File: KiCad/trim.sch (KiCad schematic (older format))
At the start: 33 parts

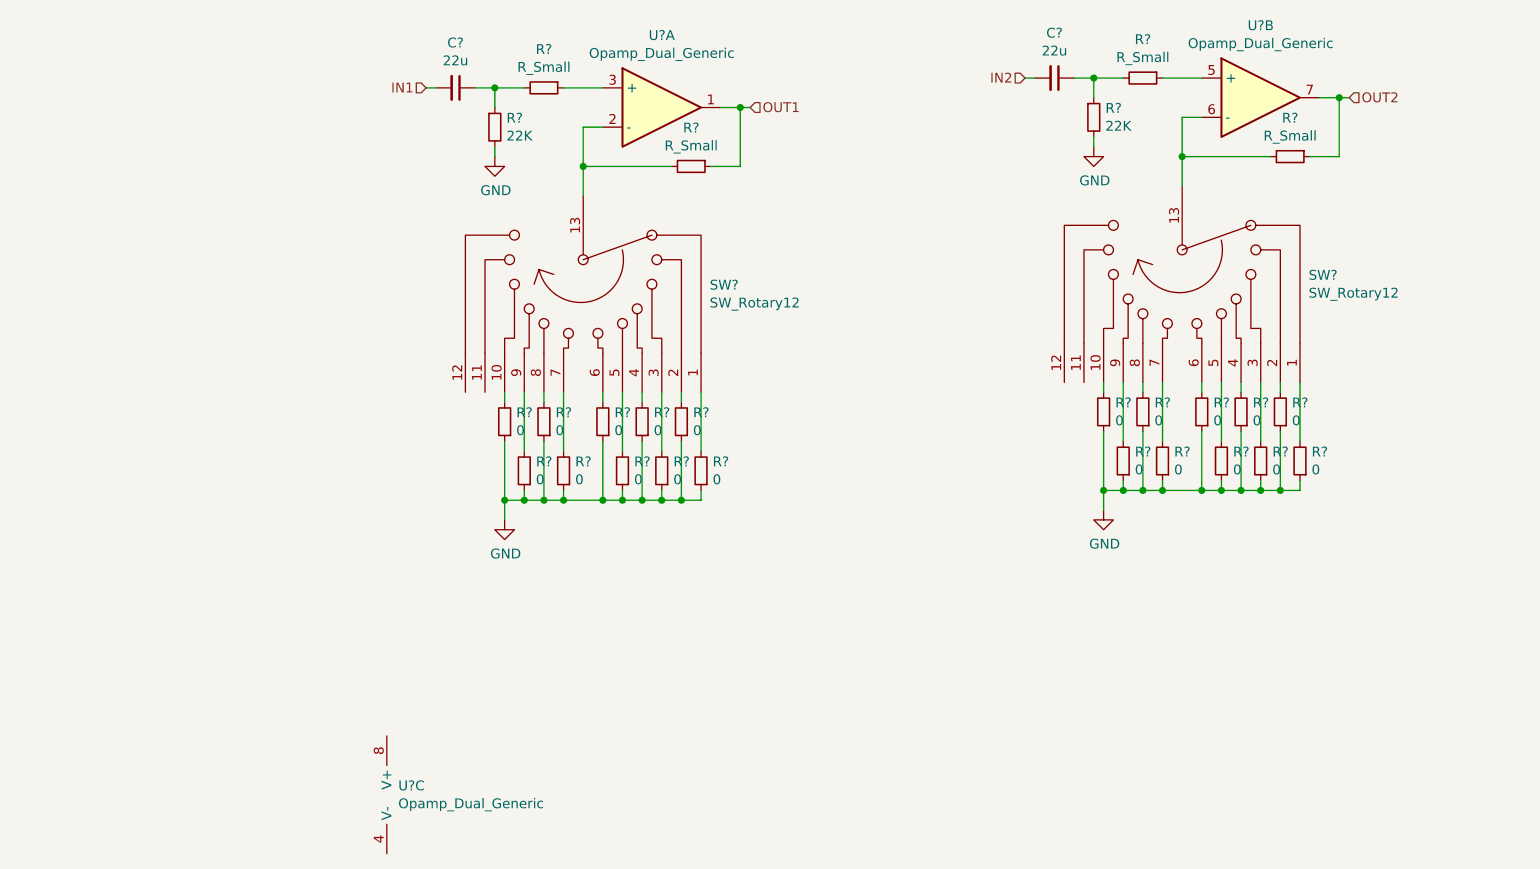
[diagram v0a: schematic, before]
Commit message: restored filter and added initial attenuation in trim
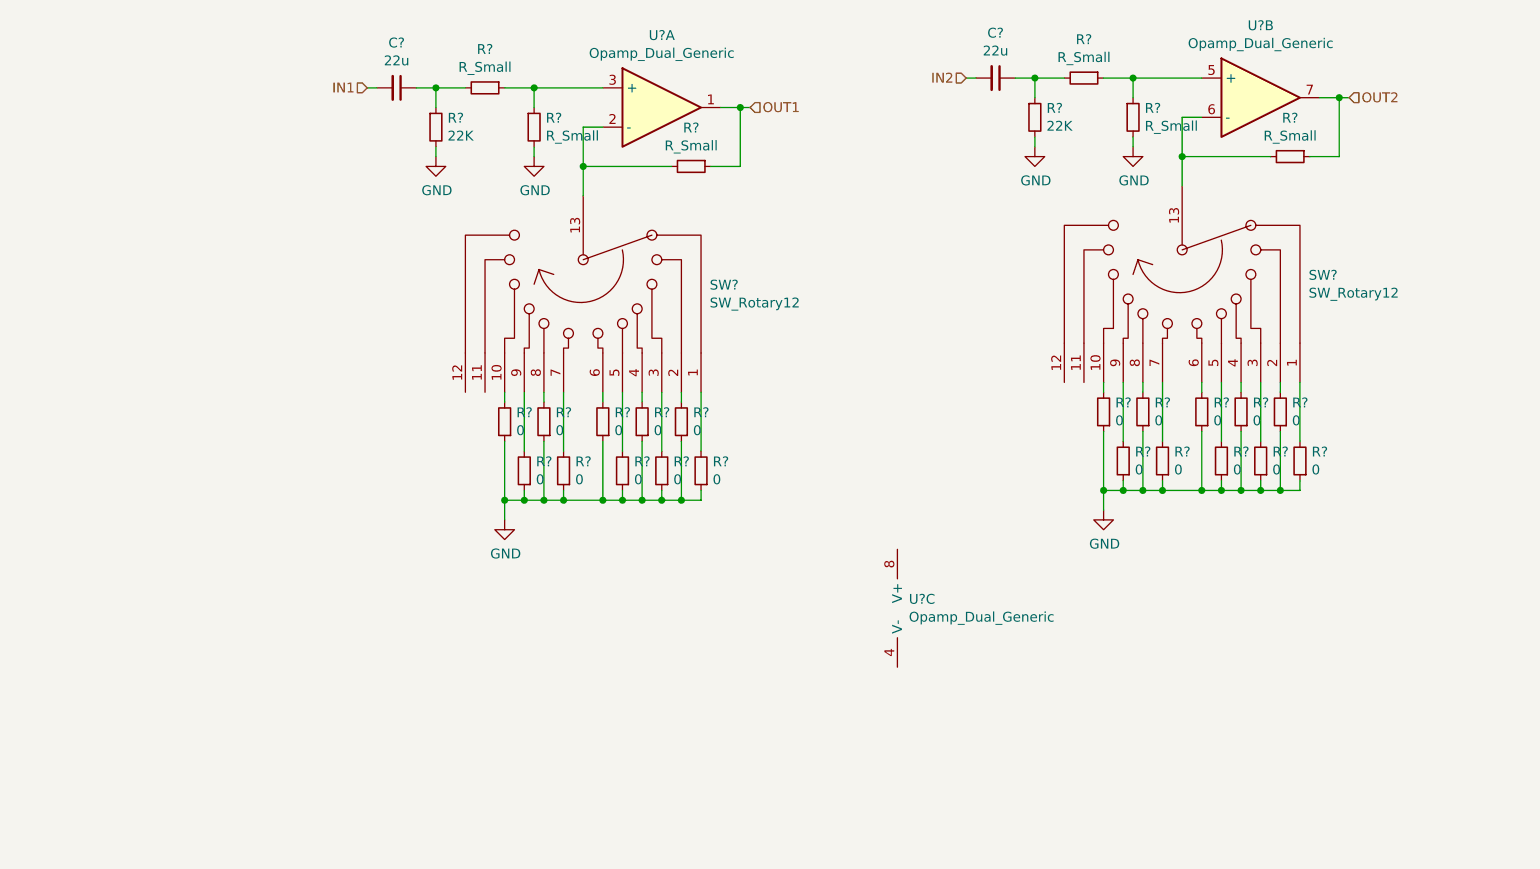
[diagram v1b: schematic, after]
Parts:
- removed R?: 22K, symbol Device:R_Small
- removed R?: R_Small, symbol Device:R_Small
- added R? (x3): R_Small, symbol Device:R_Small
- added R?: 22K, symbol Device:R_Small
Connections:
- net GND: now also R?.2, R?.2, R?.2
- net at R?.1, U?.3 (+): now also R?.1
- net at C?.1: now also R?.1, R?.2
- net at U?.5 (+): now also R?.1, R?.1
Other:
- moved on the sheet: C?, R?, U?C
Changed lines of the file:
@@
 $Descr A4 11693 8268
 encoding utf-8
-Sheet 4 4
+Sheet 4 5
 Title ""
 Date ""
@@
 L Device:C_Small C?
 U 1 1 60412D0A
-P 3650 3000
-F 0 "C?" V 3421 3000 50  0000 C CNN
-F 1 "22u" V 3512 3000 50  0000 C CNN
-F 2 "" H 3650 3000 50  0001 C CNN
-F 3 "~" H 3650 3000 50  0001 C CNN
-	1    3650 3000
+P 3350 3000
+F 0 "C?" V 3121 3000 50  0000 C CNN
+F 1 "22u" V 3212 3000 50  0000 C CNN
+F 2 "" H 3350 3000 50  0001 C CNN
+F 3 "~" H 3350 3000 50  0001 C CNN
+	1    3350 3000
 	0    1    1    0
 $EndComp
@@
 L Device:R_Small R?
 U 1 1 6041330E
-P 3850 3200
-F 0 "R?" H 3909 3246 50  0000 L CNN
-F 1 "22K" H 3909 3155 50  0000 L CNN
-F 2 "" H 3850 3200 50  0001 C CNN
-F 3 "~" H 3850 3200 50  0001 C CNN
-	1    3850 3200
-	1    0    0    -1
-$EndComp
-Wire Wire Line
-	3850 3100 3850 3000
-Wire Wire Line
-	3850 3000 3750 3000
+P 3550 3200
+F 0 "R?" H 3609 3246 50  0000 L CNN
+F 1 "22K" H 3609 3155 50  0000 L CNN
+F 2 "" H 3550 3200 50  0001 C CNN
+F 3 "~" H 3550 3200 50  0001 C CNN
+	1    3550 3200
+	1    0    0    -1
+$EndComp
+Wire Wire Line
+	3550 3100 3550 3000
+Wire Wire Line
+	3550 3000 3450 3000
 $Comp
 L power:GND #PWR?
 U 1 1 6041385B
-P 3850 3350
-F 0 "#PWR?" H 3850 3100 50  0001 C CNN
-F 1 "GND" H 3855 3177 50  0000 C CNN
-F 2 "" H 3850 3350 50  0001 C CNN
-F 3 "" H 3850 3350 50  0001 C CNN
-	1    3850 3350
-	1    0    0    -1
-$EndComp
-Wire Wire Line
-	3850 3350 3850 3300
+P 3550 3350
+F 0 "#PWR?" H 3550 3100 50  0001 C CNN
+F 1 "GND" H 3555 3177 50  0000 C CNN
+F 2 "" H 3550 3350 50  0001 C CNN
+F 3 "" H 3550 3350 50  0001 C CNN
+	1    3550 3350
+	1    0    0    -1
+$EndComp
+Wire Wire Line
+	3550 3350 3550 3300
 $Comp
 L Device:R_Small R?
 U 1 1 60413A53
-P 4100 3000
-F 0 "R?" V 3904 3000 50  0000 C CNN
-F 1 "R_Small" V 3995 3000 50  0000 C CNN
-F 2 "" H 4100 3000 50  0001 C CNN
-F 3 "~" H 4100 3000 50  0001 C CNN
-	1    4100 3000
-	0    1    1    0
-$EndComp
-Wire Wire Line
-	4000 3000 3850 3000
-Connection ~ 3850 3000
+P 3800 3000
+F 0 "R?" V 3604 3000 50  0000 C CNN
+F 1 "R_Small" V 3695 3000 50  0000 C CNN
+F 2 "" H 3800 3000 50  0001 C CNN
+F 3 "~" H 3800 3000 50  0001 C CNN
+	1    3800 3000
+	0    1    1    0
+$EndComp
+Connection ~ 3550 3000
 $Comp
 L Device:Opamp_Dual_Generic U?
@@
 $EndComp
 Wire Wire Line
-	4400 3000 4200 3000
-Wire Wire Line
 	4400 3200 4300 3200
 Wire Wire Line
@@
 L Device:C_Small C?
 U 1 1 604284FE
-P 6700 2950
-F 0 "C?" V 6471 2950 50  0000 C CNN
-F 1 "22u" V 6562 2950 50  0000 C CNN
-F 2 "" H 6700 2950 50  0001 C CNN
-F 3 "~" H 6700 2950 50  0001 C CNN
-	1    6700 2950
-	0    1    1    0
-$EndComp
-$Comp
-L Device:R_Small R?
-U 1 1 60428504
-P 6900 3150
-F 0 "R?" H 6959 3196 50  0000 L CNN
-F 1 "22K" H 6959 3105 50  0000 L CNN
-F 2 "" H 6900 3150 50  0001 C CNN
-F 3 "~" H 6900 3150 50  0001 C CNN
-	1    6900 3150
-	1    0    0    -1
-$EndComp
-Wire Wire Line
-	6900 3050 6900 2950
-Wire Wire Line
-	6900 2950 6800 2950
-$Comp
-L power:GND #PWR?
-U 1 1 6042850C
-P 6900 3300
-F 0 "#PWR?" H 6900 3050 50  0001 C CNN
-F 1 "GND" H 6905 3127 50  0000 C CNN
-F 2 "" H 6900 3300 50  0001 C CNN
-F 3 "" H 6900 3300 50  0001 C CNN
-	1    6900 3300
-	1    0    0    -1
-$EndComp
-Wire Wire Line
-	6900 3300 6900 3250
-$Comp
-L Device:R_Small R?
-U 1 1 60428513
-P 7150 2950
-F 0 "R?" V 6954 2950 50  0000 C CNN
-F 1 "R_Small" V 7045 2950 50  0000 C CNN
-F 2 "" H 7150 2950 50  0001 C CNN
-F 3 "~" H 7150 2950 50  0001 C CNN
-	1    7150 2950
-	0    1    1    0
-$EndComp
-Wire Wire Line
-	7050 2950 6900 2950
-Connection ~ 6900 2950
-Wire Wire Line
-	7450 2950 7250 2950
+P 6400 2950
+F 0 "C?" V 6171 2950 50  0000 C CNN
+F 1 "22u" V 6262 2950 50  0000 C CNN
+F 2 "" H 6400 2950 50  0001 C CNN
+F 3 "~" H 6400 2950 50  0001 C CNN
+	1    6400 2950
+	0    1    1    0
+$EndComp
 Wire Wire Line
 	7450 3150 7350 3150
@@
 Wire Wire Line
 	6950 5050 7050 5050
-Text HLabel 3500 3000 0    50   Input ~ 0
+Text HLabel 3200 3000 0    50   Input ~ 0
 IN1
 Wire Wire Line
-	3500 3000 3550 3000
+	3200 3000 3250 3000
 Text HLabel 5150 3100 2    50   Input ~ 0
 OUT1
@@
 	5150 3100 5100 3100
 Connection ~ 5100 3100
-Text HLabel 6550 2950 0    50   Input ~ 0
+Text HLabel 6250 2950 0    50   Input ~ 0
 IN2
 Wire Wire Line
-	6550 2950 6600 2950
+	6250 2950 6300 2950
 Text HLabel 8200 3050 2    50   Input ~ 0
 OUT2
@@
 L Device:Opamp_Dual_Generic U?
 U 3 1 60459ACB
-P 3400 6600
-F 0 "U?" H 3358 6646 50  0000 L CNN
-F 1 "Opamp_Dual_Generic" H 3358 6555 50  0000 L CNN
-F 2 "" H 3400 6600 50  0001 C CNN
-F 3 "~" H 3400 6600 50  0001 C CNN
-	3    3400 6600
-	1    0    0    -1
-$EndComp
+P 6000 5650
+F 0 "U?" H 5958 5696 50  0000 L CNN
+F 1 "Opamp_Dual_Generic" H 5958 5605 50  0000 L CNN
+F 2 "" H 6000 5650 50  0001 C CNN
+F 3 "~" H 6000 5650 50  0001 C CNN
+	3    6000 5650
+	1    0    0    -1
+$EndComp
+$Comp
+L Device:R_Small R?
+U 1 1 6049EE8B
+P 4050 3200
+F 0 "R?" H 4109 3246 50  0000 L CNN
+F 1 "R_Small" H 4109 3155 50  0000 L CNN
+F 2 "" H 4050 3200 50  0001 C CNN
+F 3 "~" H 4050 3200 50  0001 C CNN
+	1    4050 3200
+	1    0    0    -1
+$EndComp
+Wire Wire Line
+	4050 3100 4050 3000
+$Comp
+L power:GND #PWR?
+U 1 1 6049EE92
+P 4050 3350
+F 0 "#PWR?" H 4050 3100 50  0001 C CNN
+F 1 "GND" H 4055 3177 50  0000 C CNN
+F 2 "" H 4050 3350 50  0001 C CNN
+F 3 "" H 4050 3350 50  0001 C CNN
+	1    4050 3350
+	1    0    0    -1
+$EndComp
+Wire Wire Line
+	4050 3350 4050 3300
+Wire Wire Line
+	3900 3000 4050 3000
+Connection ~ 4050 3000
+Wire Wire Line
+	4050 3000 4400 3000
+Wire Wire Line
+	3550 3000 3700 3000
+$Comp
+L Device:R_Small R?
+U 1 1 604B93C5
+P 6600 3150
+F 0 "R?" H 6659 3196 50  0000 L CNN
+F 1 "22K" H 6659 3105 50  0000 L CNN
+F 2 "" H 6600 3150 50  0001 C CNN
+F 3 "~" H 6600 3150 50  0001 C CNN
+	1    6600 3150
+	1    0    0    -1
+$EndComp
+Wire Wire Line
+	6600 3050 6600 2950
+Wire Wire Line
+	6600 2950 6500 2950
+$Comp
+L power:GND #PWR?
+U 1 1 604B93CD
+P 6600 3300
+F 0 "#PWR?" H 6600 3050 50  0001 C CNN
+F 1 "GND" H 6605 3127 50  0000 C CNN
+F 2 "" H 6600 3300 50  0001 C CNN
+F 3 "" H 6600 3300 50  0001 C CNN
+	1    6600 3300
+	1    0    0    -1
+$EndComp
+Wire Wire Line
+	6600 3300 6600 3250
+$Comp
+L Device:R_Small R?
+U 1 1 604B93D4
+P 6850 2950
+F 0 "R?" V 6654 2950 50  0000 C CNN
+F 1 "R_Small" V 6745 2950 50  0000 C CNN
+F 2 "" H 6850 2950 50  0001 C CNN
+F 3 "~" H 6850 2950 50  0001 C CNN
+	1    6850 2950
+	0    1    1    0
+$EndComp
+Connection ~ 6600 2950
+$Comp
+L Device:R_Small R?
+U 1 1 604B93DB
+P 7100 3150
+F 0 "R?" H 7159 3196 50  0000 L CNN
+F 1 "R_Small" H 7159 3105 50  0000 L CNN
+F 2 "" H 7100 3150 50  0001 C CNN
+F 3 "~" H 7100 3150 50  0001 C CNN
+	1    7100 3150
+	1    0    0    -1
+$EndComp
+Wire Wire Line
+	7100 3050 7100 2950
+$Comp
+L power:GND #PWR?
+U 1 1 604B93E2
+P 7100 3300
+F 0 "#PWR?" H 7100 3050 50  0001 C CNN
+F 1 "GND" H 7105 3127 50  0000 C CNN
+F 2 "" H 7100 3300 50  0001 C CNN
+F 3 "" H 7100 3300 50  0001 C CNN
+	1    7100 3300
+	1    0    0    -1
+$EndComp
+Wire Wire Line
+	7100 3300 7100 3250
+Wire Wire Line
+	6950 2950 7100 2950
+Connection ~ 7100 2950
+Wire Wire Line
+	7100 2950 7450 2950
+Wire Wire Line
+	6600 2950 6750 2950
 $EndSCHEMATC

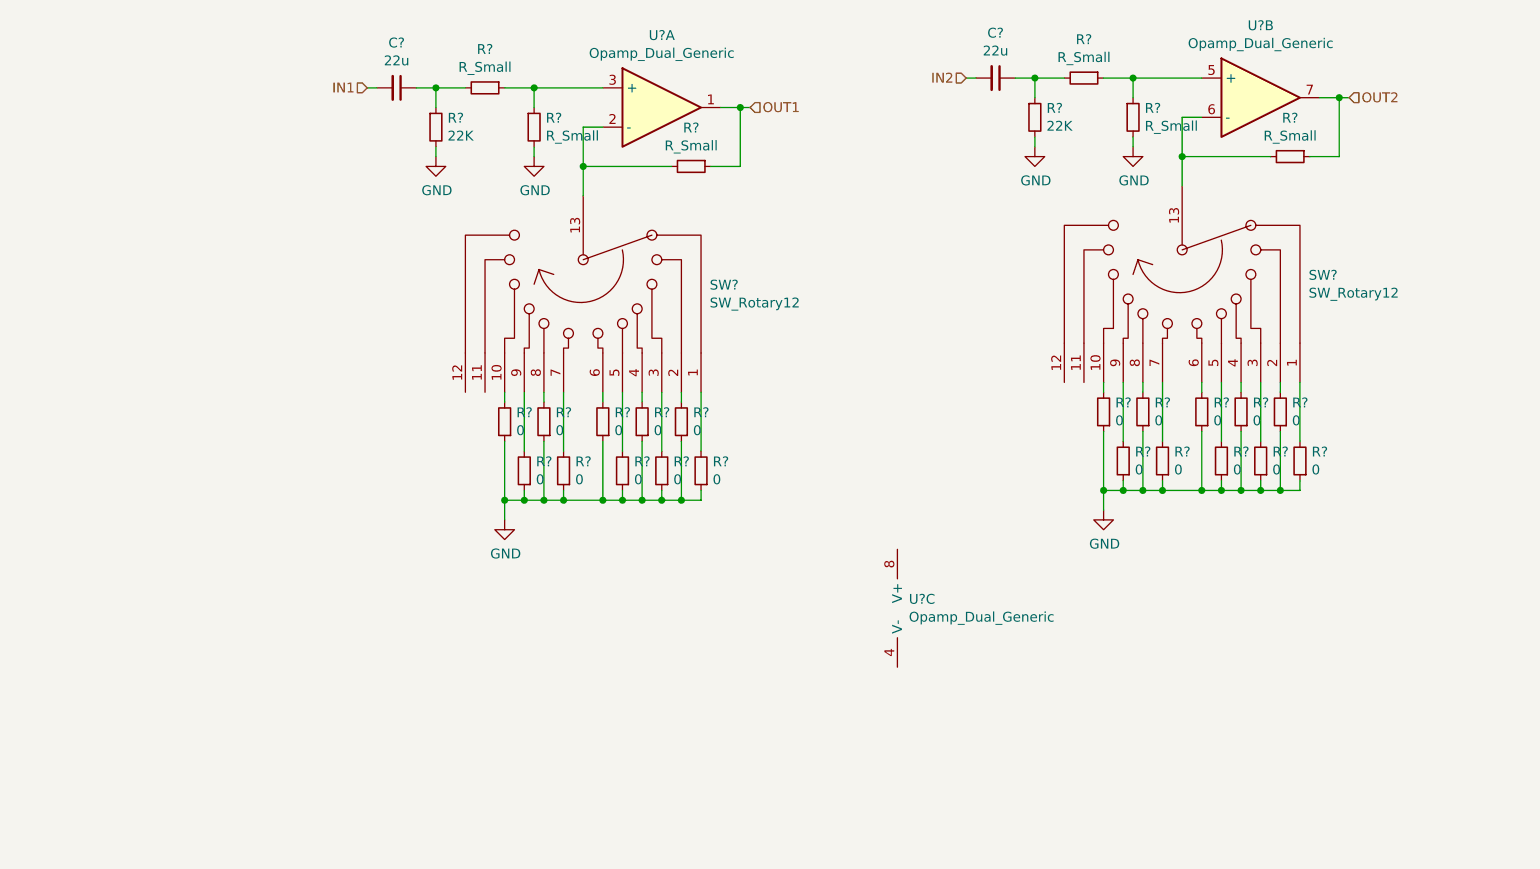
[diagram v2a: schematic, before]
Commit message: moved initial attenuation to filter input
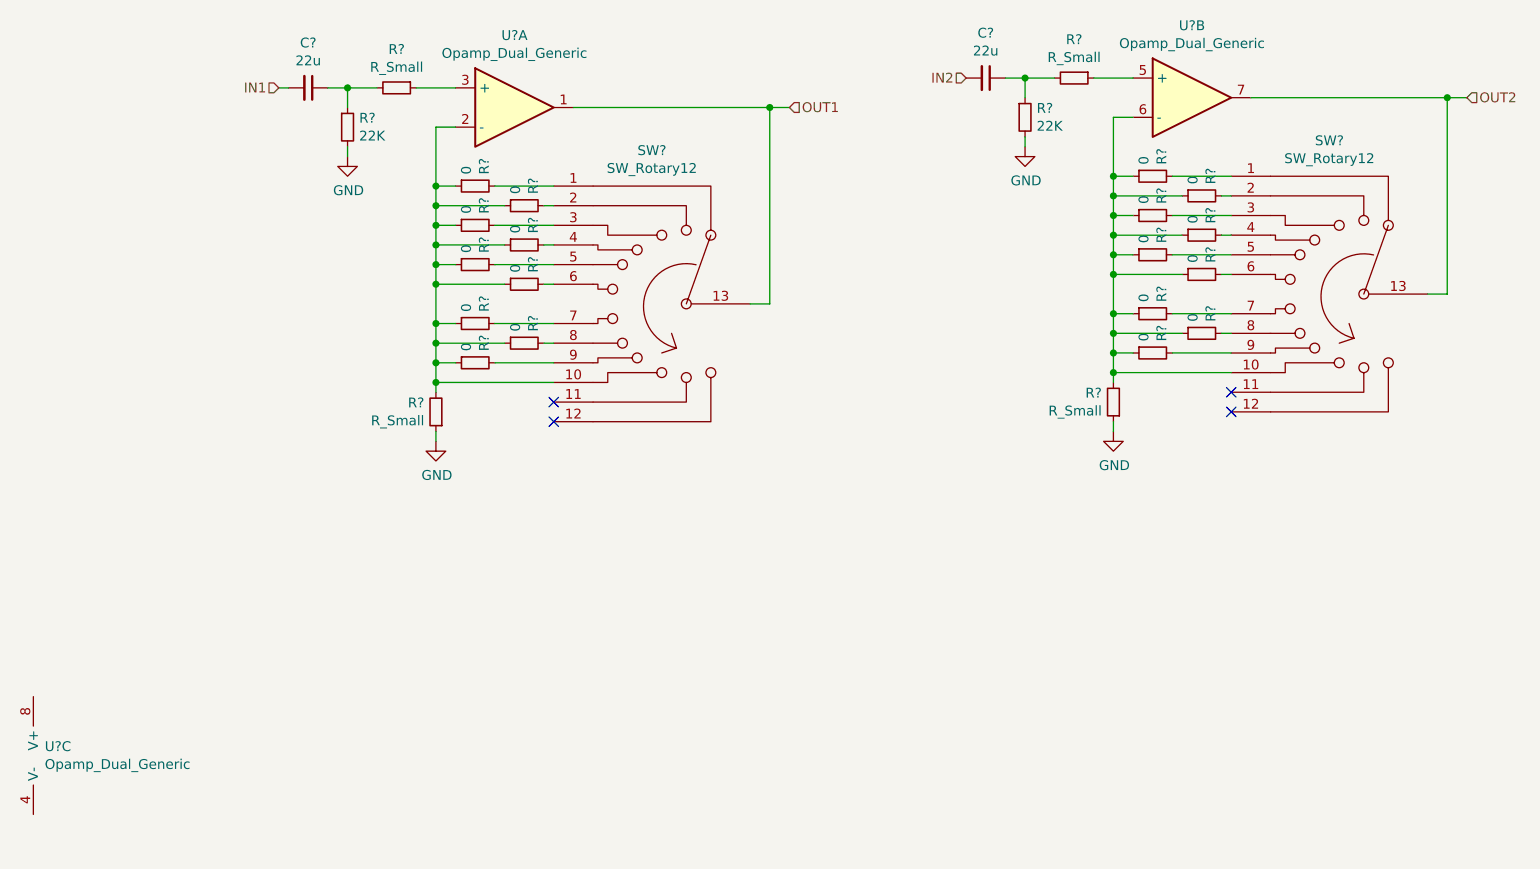
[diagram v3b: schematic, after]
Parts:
- removed C?: 22u, symbol Device:C_Small
- removed R? (x11): 0, symbol Device:R_Small
- removed R? (x4): R_Small, symbol Device:R_Small
- removed R?: 22K, symbol Device:R_Small
- removed SW?: SW_Rotary12, symbol Switch:SW_Rotary12
- added C?: 22u, symbol Device:C_Small
- added R?: 22K, symbol Device:R_Small
- added R? (x2): R_Small, symbol Device:R_Small
- added R? (x9): 0, symbol Device:R_Small
- added SW?: SW_Rotary12, symbol Switch:SW_Rotary12
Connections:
- net GND: now also R?.1, R?.1, R?.2; no longer R?.1, R?.1, R?.1, R?.1, R?.1, R?.1, R?.1, R?.1, R?.1
- net IN2: now also C?.2
- net OUT1: now also SW?.13; no longer R?.1
- net OUT2: now also SW?.13
- net at R?.2, U?.2 (-): now also R?.1, R?.1, R?.1, R?.1, R?.1, R?.1, R?.1, R?.1, R?.1, SW?.10; no longer SW?.13
- net at U?.6 (-): now also R?.1, R?.1, R?.1, R?.1, R?.1, R?.1, R?.1, R?.1, R?.1, R?.2, SW?.10
- net at U?.5 (+): now also R?.1
- new net: C?.1, R?.1, R?.2
- new net: R?.2, SW?.9
- new net: R?.2, SW?.8
- new net: R?.2, SW?.7
- new net: R?.2, SW?.6
- new net: R?.2, SW?.5
- new net: R?.2, SW?.4
- new net: R?.2, SW?.3
- new net: R?.2, SW?.2
- new net: R?.2, SW?.1
- no-connect marks 0 -> 4
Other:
- moved on the sheet: C?, R?, SW?, U?A, U?B, U?C

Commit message: saved from laptop and added new questions
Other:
- moved on the sheet: U?C
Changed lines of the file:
@@
 L Device:Opamp_Dual_Generic U?
 U 3 1 60459ACB
-P 1600 6400
-F 0 "U?" H 1558 6446 50  0000 L CNN
-F 1 "Opamp_Dual_Generic" H 1558 6355 50  0000 L CNN
-F 2 "" H 1600 6400 50  0001 C CNN
-F 3 "~" H 1600 6400 50  0001 C CNN
-	3    1600 6400
+P 5900 5400
+F 0 "U?" H 5858 5446 50  0000 L CNN
+F 1 "Opamp_Dual_Generic" H 5858 5355 50  0000 L CNN
+F 2 "" H 5900 5400 50  0001 C CNN
+F 3 "~" H 5900 5400 50  0001 C CNN
+	3    5900 5400
 	1    0    0    -1
 $EndComp
